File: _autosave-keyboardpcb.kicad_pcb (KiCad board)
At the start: 2 copper layers, 70.1 x 40.2 mm, 24 parts, among them SW1 SW_Push, U1 ATmega32U4-A, Y1 16MHz

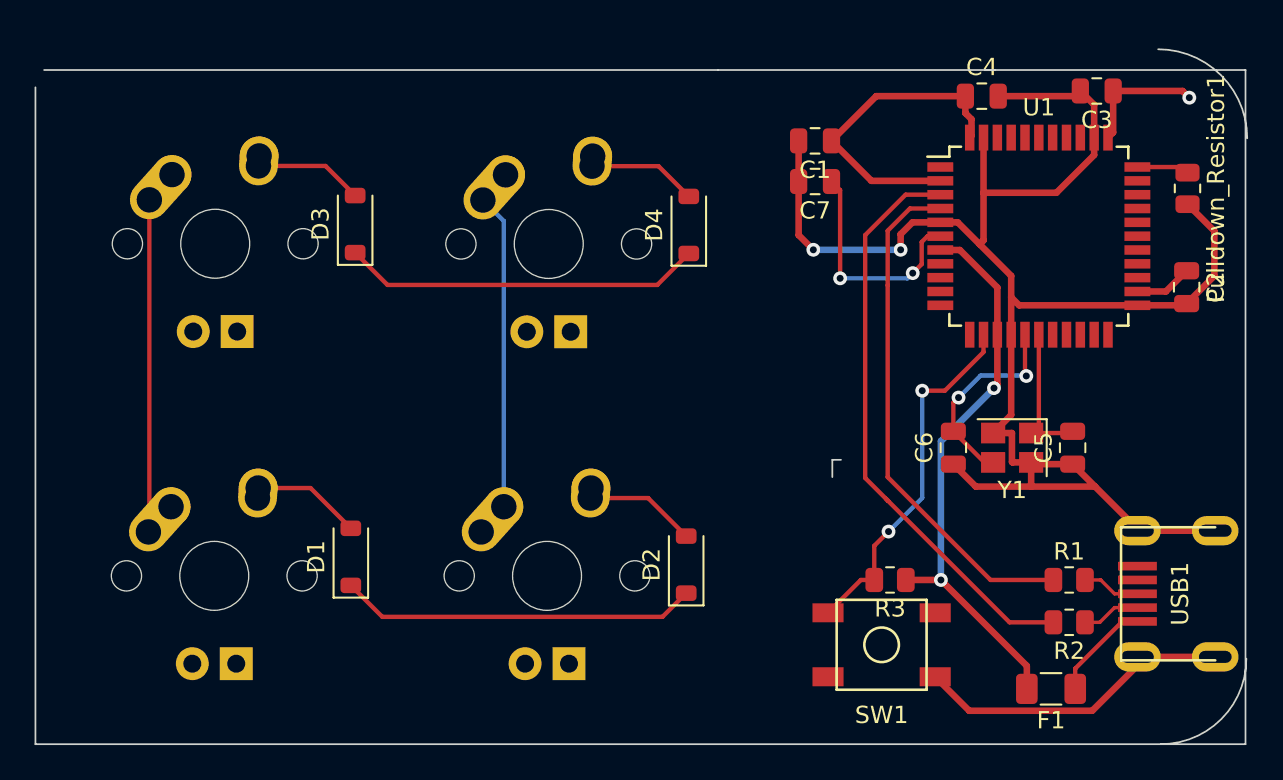
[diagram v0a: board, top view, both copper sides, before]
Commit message: finished pcb routing
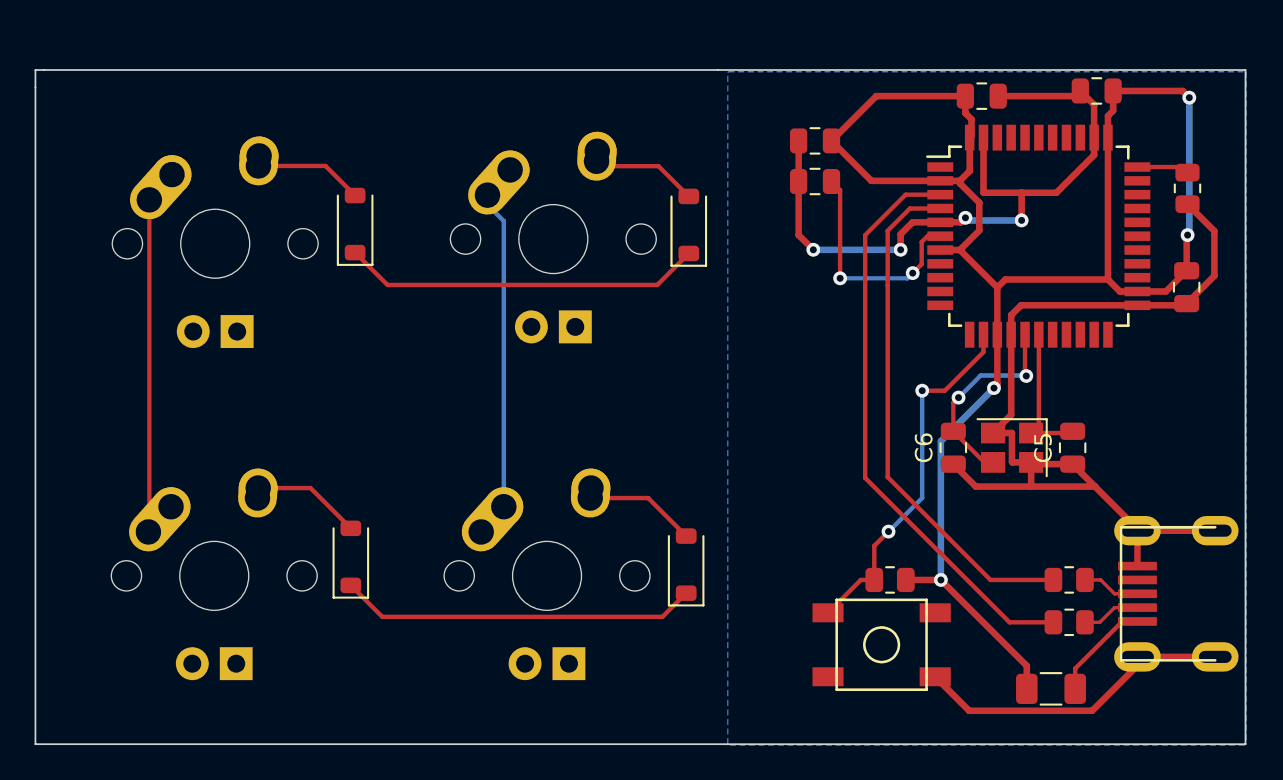
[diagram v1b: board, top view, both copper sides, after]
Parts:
- moved MX2 0.39 mm to (140.0, 75.8)
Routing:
- net +5V: track 62.3 -> 97.9 mm, vias 3 -> 4
- net GND: track 115.0 -> 112.8 mm, vias 2 -> 4
- net Net-(D1-A): track 6.33 -> 6.92 mm
- added copper zone on B.Cu, net GND
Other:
- board size 70.1 x 40.2 mm -> 70 x 39 mm
